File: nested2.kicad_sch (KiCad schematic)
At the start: 14 parts, among them Q2 PMOS, Q3 AO3400A, Q4 AO3400A, Q5 PMOS

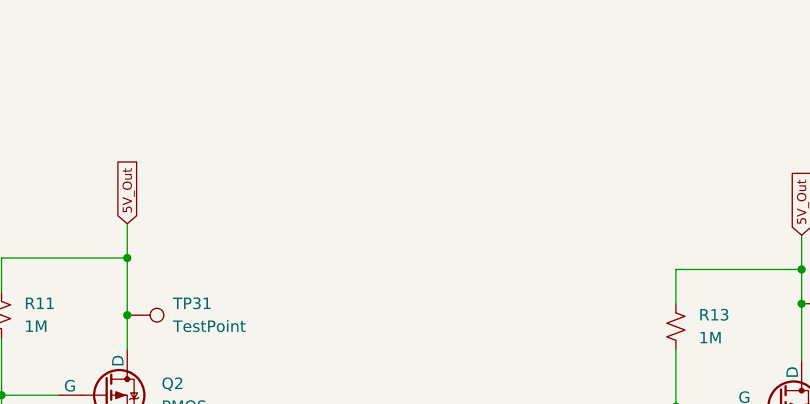
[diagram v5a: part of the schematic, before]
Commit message: Removed old backups and updated KiCad files
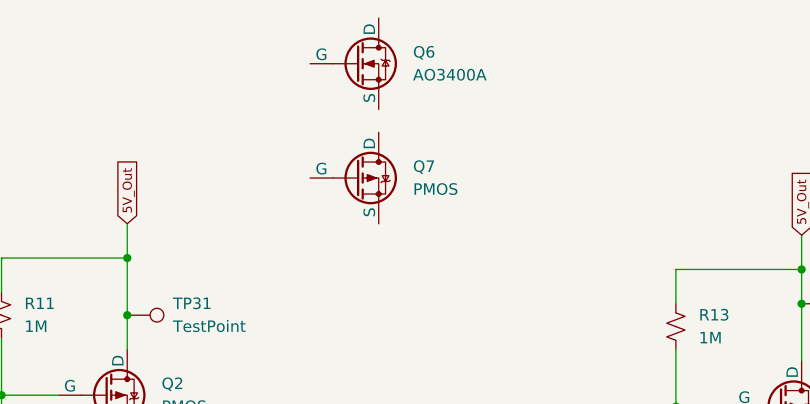
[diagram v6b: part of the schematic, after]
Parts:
- added Q6: AO3400A, Package_TO_SOT_SMD:SOT-23-3, symbol Simulation_SPICE:NMOS
- added Q7: PMOS, Package_TO_SOT_SMD:SOT-23_Handsoldering, symbol Simulation_SPICE:PMOS
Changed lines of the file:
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@@
+	)
+	(symbol
+		(lib_id "Simulation_SPICE:NMOS")
+		(at 184.15 92.71 0)
+		(unit 1)
+		(exclude_from_sim no)
+		(in_bom yes)
+		(on_board yes)
+		(dnp no)
+		(fields_autoplaced yes)
+		(property "Reference" "Q6"
+			(at 190.5 91.4399 0)
+			(effects
+				(font
+					(size 1.27 1.27)
+				)
+				(justify left)
+			)
+		)
+		(property "Value" "AO3400A"
+			(at 190.5 93.9799 0)
+			(effects
+				(font
+					(size 1.27 1.27)
+				)
+				(justify left)
+			)
+		)
+		(property "Footprint" "Package_TO_SOT_SMD:SOT-23-3"
+			(at 189.23 90.17 0)
+			(effects
+				(font
+					(size 1.27 1.27)
+				)
+				(hide yes)
+			)
+		)
+		(property "Datasheet" "https://ngspice.sourceforge.io/docs/ngspice-html-manual/manual.xhtml#cha_MOSFETs"
+			(at 184.15 105.41 0)
+			(effects
+				(font
+					(size 1.27 1.27)
+				)
+				(hide yes)
+			)
+		)
+		(property "Description" "N-MOSFET transistor, drain/source/gate"
+			(at 184.15 92.71 0)
+			(effects
+				(font
+					(size 1.27 1.27)
+				)
+				(hide yes)
+			)
+		)
+		(property "Sim.Device" "NMOS"
+			(at 184.15 109.855 0)
+			(effects
+				(font
+					(size 1.27 1.27)
+				)
+				(hide yes)
+			)
+		)
+		(property "Sim.Type" "VDMOS"
+			(at 184.15 111.76 0)
+			(effects
+				(font
+					(size 1.27 1.27)
+				)
+				(hide yes)
+			)
+		)
+		(property "Sim.Pins" "1=D 2=G 3=S"
+			(at 184.15 107.95 0)
+			(effects
+				(font
+					(size 1.27 1.27)
+				)
+				(hide yes)
+			)
+		)
+		(property "LCSC" "C20917"
+			(at 184.15 92.71 0)
+			(effects
+				(font
+					(size 1.27 1.27)
+				)
+				(hide yes)
+			)
+		)
+		(pin "2"
+		)
+		(pin "1"
+		)
+		(pin "3"
+		)
+		(instances
+			(project "EEE3088F Design project"
+				(path "/d1463c6f-2f5e-4460-8cd2-c7ccf4d8def7/5921a43a-66b4-4a5d-9407-3d9130778733"
+					(reference "Q6")
+					(unit 1)
+				)
+			)
+		)
 	)
 	(symbol
@@
 					(unit 1)
 				)
+			)
+		)
+	)
+	(symbol
+		(lib_id "Simulation_SPICE:PMOS")
+		(at 184.15 105.41 0)
+		(unit 1)
+		(exclude_from_sim no)
+		(in_bom yes)
+		(on_board yes)
+		(dnp no)
+		(fields_autoplaced yes)
+		(property "Reference" "Q7"
+			(at 190.5 104.1399 0)
+			(effects
+				(font
+					(size 1.27 1.27)
+				)
+				(justify left)
+			)
+		)
+		(property "Value" "PMOS"
+			(at 190.5 106.6799 0)
+			(effects
+				(font
+					(size 1.27 1.27)
+				)
+				(justify left)
+			)
+		)
+		(property "Footprint" "Package_TO_SOT_SMD:SOT-23_Handsoldering"
+			(at 189.23 102.87 0)
+			(effects
+				(font
+					(size 1.27 1.27)
+				)
+				(hide yes)
+			)
+		)
+		(property "Datasheet" "https://ngspice.sourceforge.io/docs/ngspice-html-manual/manual.xhtml#cha_MOSFETs"
+			(at 184.15 118.11 0)
+			(effects
+				(font
+					(size 1.27 1.27)
+				)
+				(hide yes)
+			)
+		)
+		(property "Description" "P-MOSFET transistor, drain/source/gate"
+			(at 184.15 105.41 0)
+			(effects
+				(font
+					(size 1.27 1.27)
+				)
+				(hide yes)
+			)
+		)
+		(property "Sim.Device" "PMOS"
+			(at 184.15 122.555 0)
+			(effects
+				(font
+					(size 1.27 1.27)
+				)
+				(hide yes)
+			)
+		)
+		(property "Sim.Type" "VDMOS"
+			(at 184.15 124.46 0)
+			(effects
+				(font
+					(size 1.27 1.27)
+				)
+				(hide yes)
+			)
+		)
+		(property "Sim.Pins" "1=D 2=G 3=S"
+			(at 184.15 120.65 0)
+			(effects
+				(font
+					(size 1.27 1.27)
+				)
+				(hide yes)
+			)
+		)
+		(property "LCSC" "C15127"
+			(at 184.15 105.41 0)
+			(effects
+				(font
+					(size 1.27 1.27)
+				)
+				(hide yes)
+			)
+		)
+		(pin "3"
+		)
+		(pin "2"
+		)
+		(pin "1"
+		)
+		(instances
+			(project "EEE3088F Design project"
+				(path "/d1463c6f-2f5e-4460-8cd2-c7ccf4d8def7/5921a43a-66b4-4a5d-9407-3d9130778733"
+					(reference "Q7")
+					(unit 1)
+				)

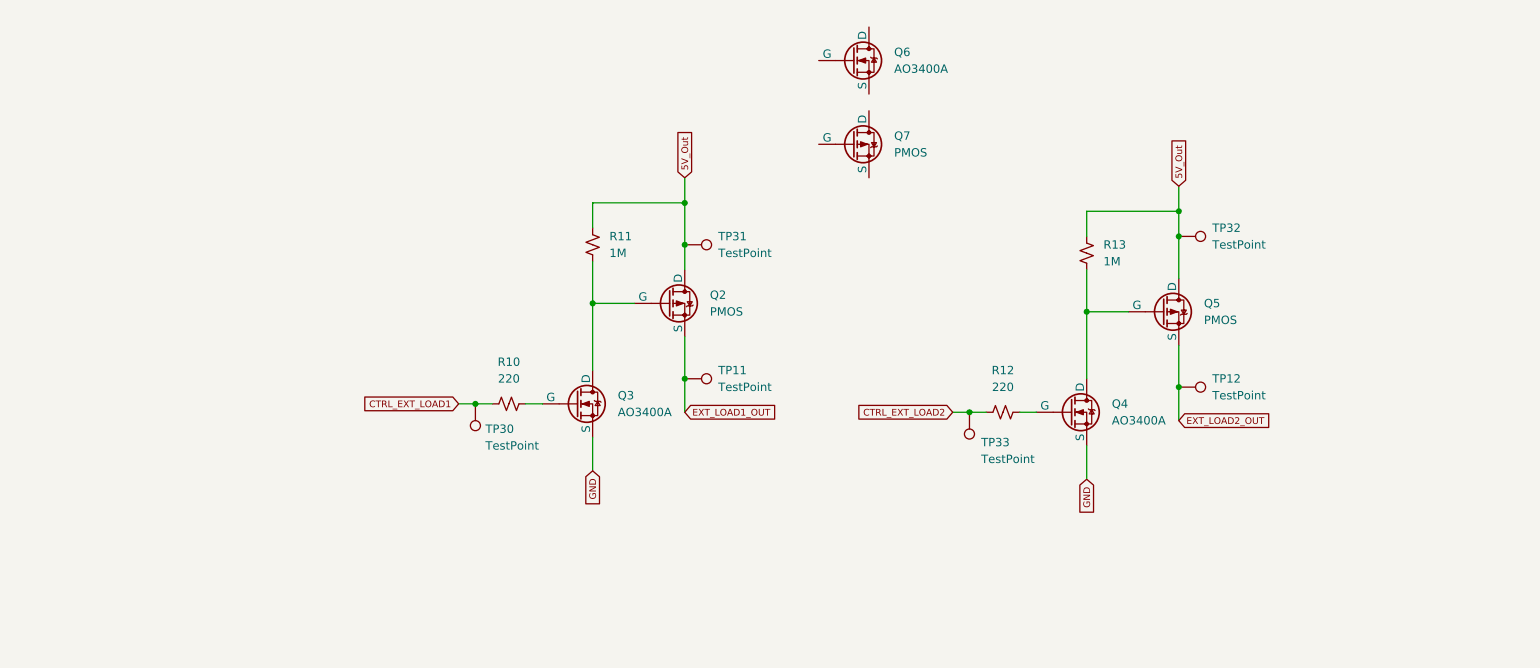
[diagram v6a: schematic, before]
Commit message: Removed old backups and updated KiCad files
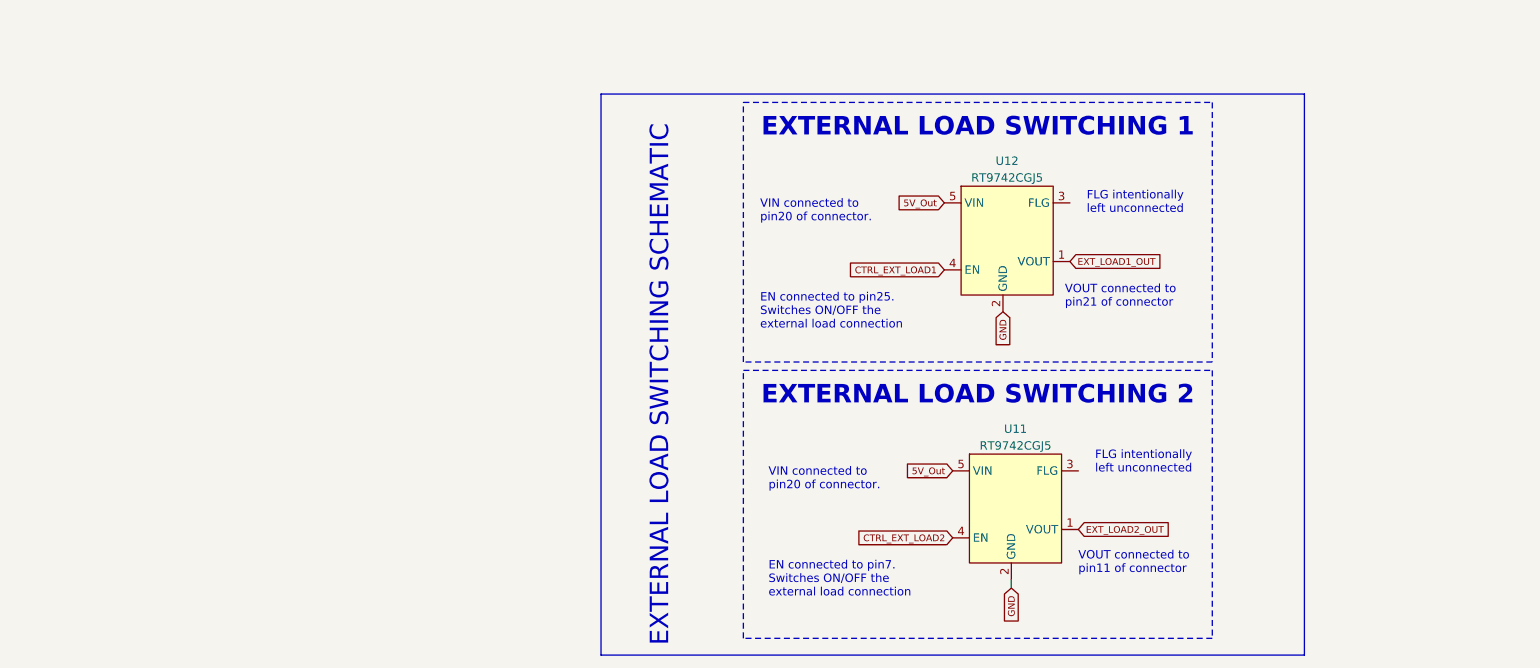
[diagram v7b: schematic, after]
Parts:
- removed Q2, Q5, Q7: PMOS, Package_TO_SOT_SMD:SOT-23_Handsoldering, symbol Simulation_SPICE:PMOS
- removed Q3, Q4, Q6: AO3400A, Package_TO_SOT_SMD:SOT-23-3, symbol Simulation_SPICE:NMOS
- removed R10, R12: 220, Resistor_SMD:R_0603_1608Metric_Pad0.98x0.95mm_HandSolder, symbol Device:R_Small_US
- removed R11, R13: 1M, Resistor_SMD:R_1206_3216Metric_Pad1.30x1.75mm_HandSolder, symbol Device:R_Small_US
- removed TP11, TP12, TP30, TP31, TP32, TP33: TestPoint, TestPoint:TestPoint_Pad_1.0x1.0mm, symbol Connector:TestPoint
- added U11, U12: RT9742CGJ5, Package_TO_SOT_SMD:TSOT-23-5, symbol HIGH SIDE SWITCH:RT9742CGJ5
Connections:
- net 5V_Out: now also U11.5 (VIN), U12.5 (VIN)
- net CTRL_EXT_LOAD1: now also U12.4 (EN)
- net CTRL_EXT_LOAD2: now also U11.4 (EN)
- net EXT_LOAD1_OUT: now also U12.1 (VOUT)
- net EXT_LOAD2_OUT: now also U11.1 (VOUT)
- net GND: now also U11.2 (GND), U12.2 (GND)
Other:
- note added: "EN connected to pin25. Switches ON/OFF the external load connection"
- note added: "EN connected to pin7. Switches ON/OFF the external load connection"
- note added: "EXTERNAL LOAD SWITCHING 1"
- note added: "EXTERNAL LOAD SWITCHING 2"
- note added: "EXTERNAL LOAD SWITCHING SCHEMATIC"
- note added: "FLG intentionally left unconnected"
- note added: "VIN connected to pin20 of connector."
- note added: "VOUT connected to pin11 of connector"
- note added: "VOUT connected to pin21 of connector"
- title: (none) -> MICRO-MOUSE POWER SUBSYSTEM
